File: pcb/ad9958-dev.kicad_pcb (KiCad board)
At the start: 4 copper layers, 40 x 32 mm, 88 parts, among them J1 INTERFACE, J2 5V, J3 OUT1, J4 OUT0, U1 LM1117-1v8-SOT223, U2 AD9958, U3 LMH6714, U4 LMH6714, X1 25 MHz

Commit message: Prefab signoffs - CP
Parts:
- U1: value LM1117-1v8-SOT223 -> AZ1117CH-1.8TRG1
- U3, U4: value LMH6714 -> LMH6714MF
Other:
- board text added: "2014-10-28 CP"
- board text added: "DRC"
- board text added: "GERBER"
- board text added: "PREFAB SIGNOFFS"

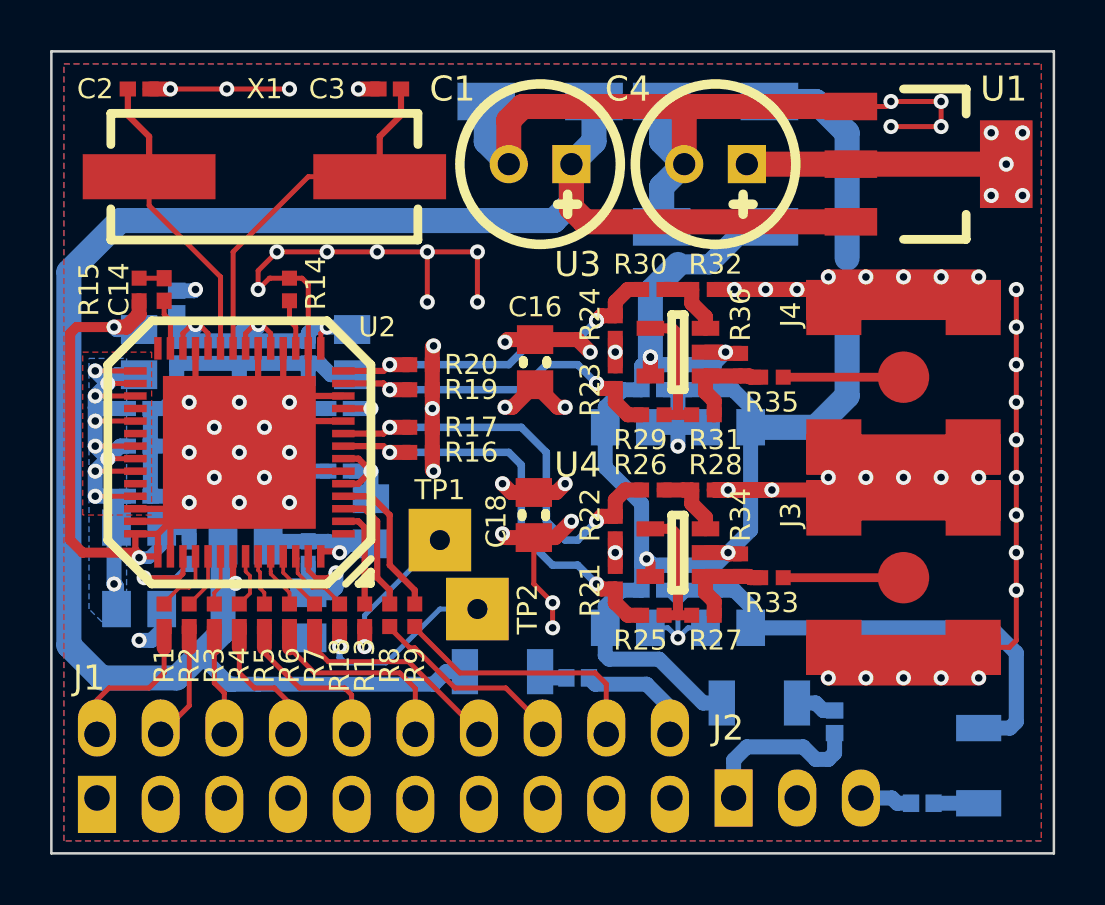
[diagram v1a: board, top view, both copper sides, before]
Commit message: Adjusted diff pair routing
Minor PCB appearance tweak
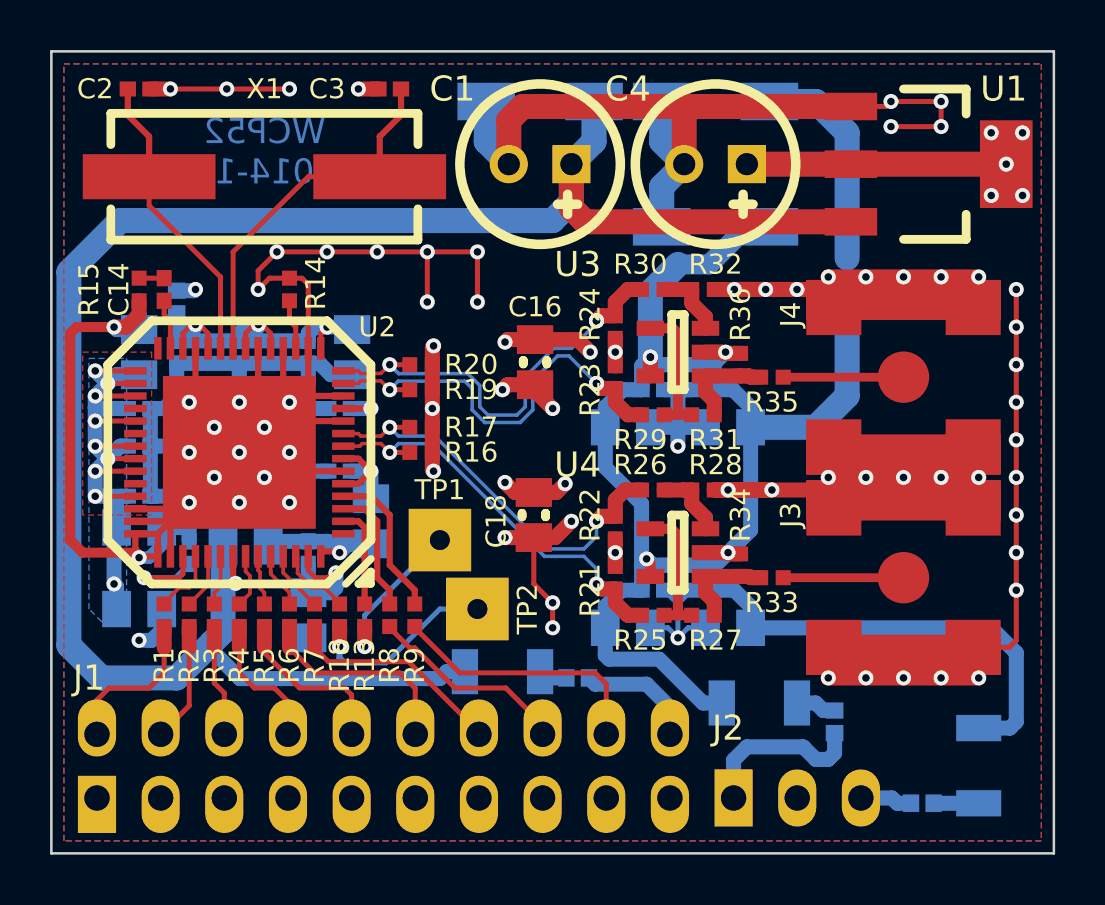
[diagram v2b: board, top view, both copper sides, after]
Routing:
- net /C1N: track 14.4 -> 17.9 mm
- net /C1P: track 14.4 -> 17.4 mm
- net /C0N: track 17.6 -> 16.7 mm
- net /C0P: track 17.5 -> 16.6 mm
- net +1.8A: track 64.6 -> 64.0 mm
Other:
- net class DiffPair added: clearance 0.1584, trace_width 0.2, via_dia 1, via_drill 0.7
- board text added: "2014-10-29 CP"
- board text added: "SYNTH REV A"
- board text added: "WCP52 2014-10"
- board text removed: "2014-10-28 CP"
- board text removed: "WCP52 GAIN/PHASE SYNTHESIZER PROTO OCT 2014"
